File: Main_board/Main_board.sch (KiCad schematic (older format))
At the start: 29 parts, among them U1 ATmega328-AU, U2 74LVC2G08, U3 74LVC2G08, Y1 20Mhz

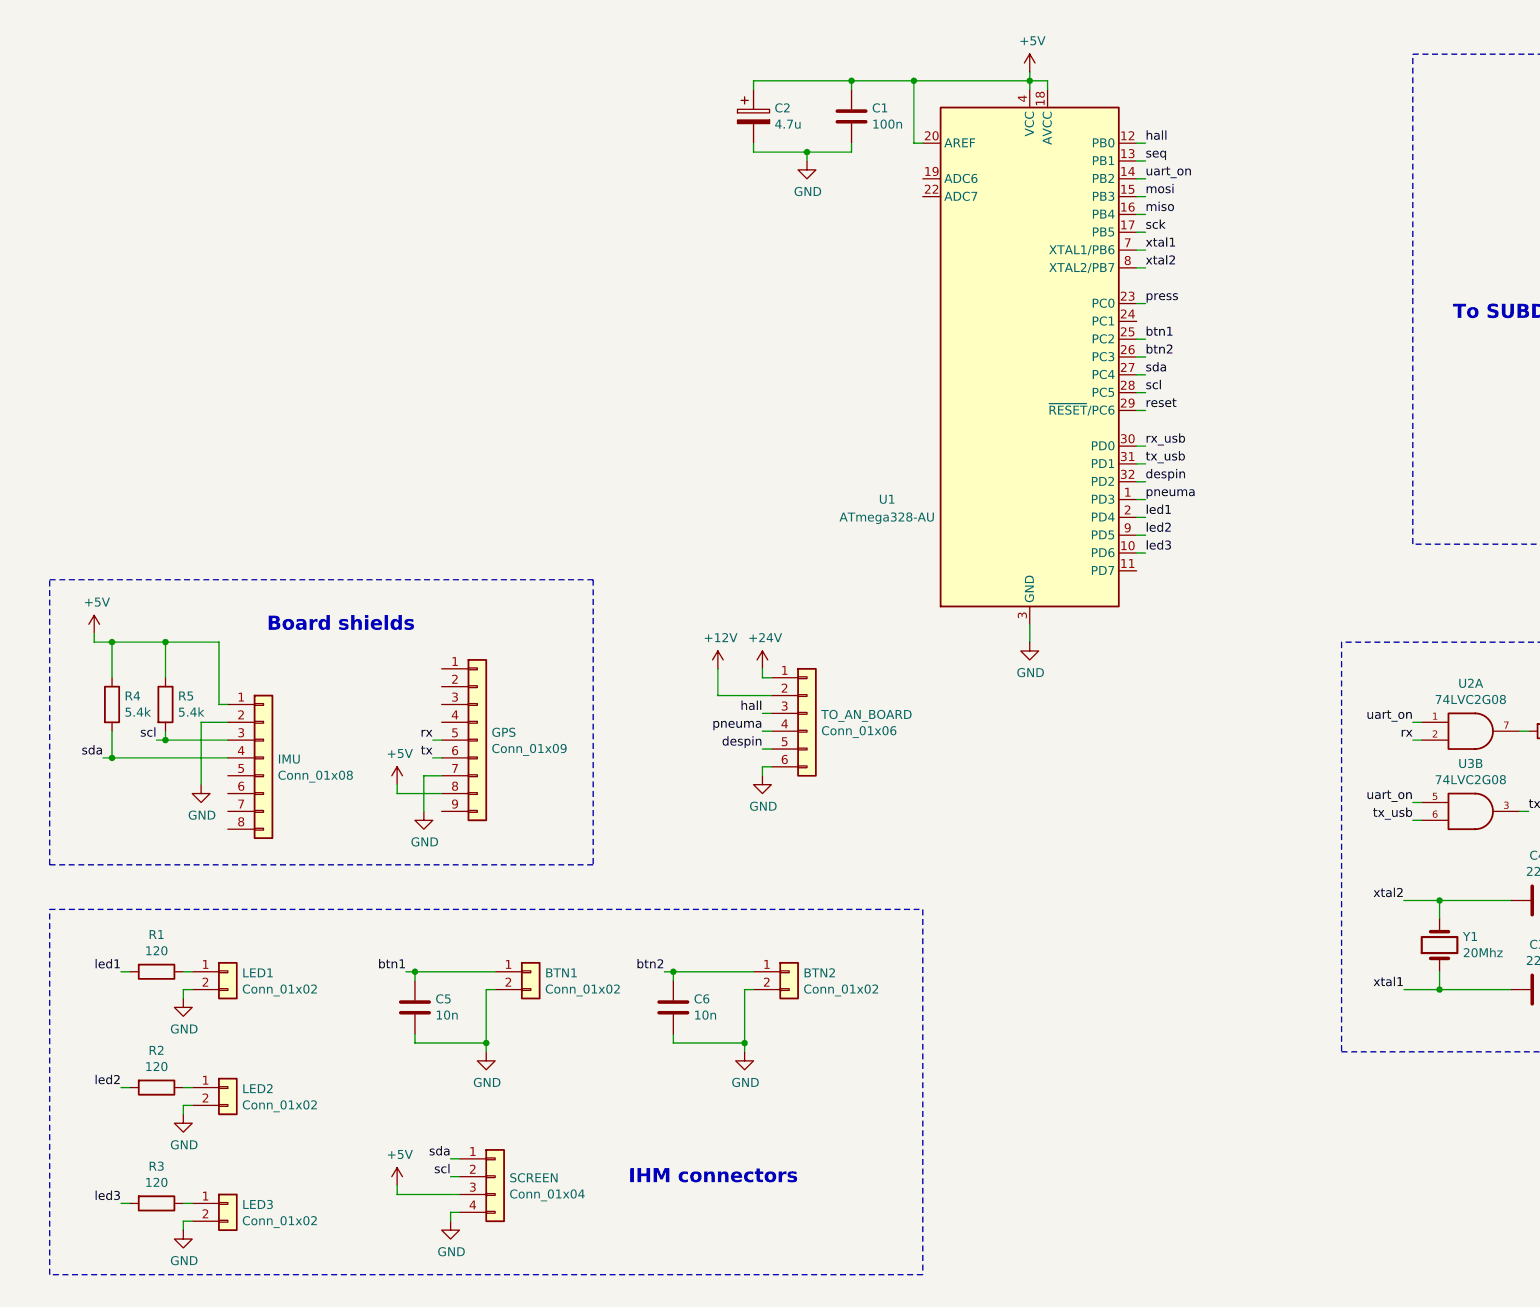
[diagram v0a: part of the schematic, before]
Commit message: ENH: Added VCO, voltage translator and flash chip libs and associated circuits
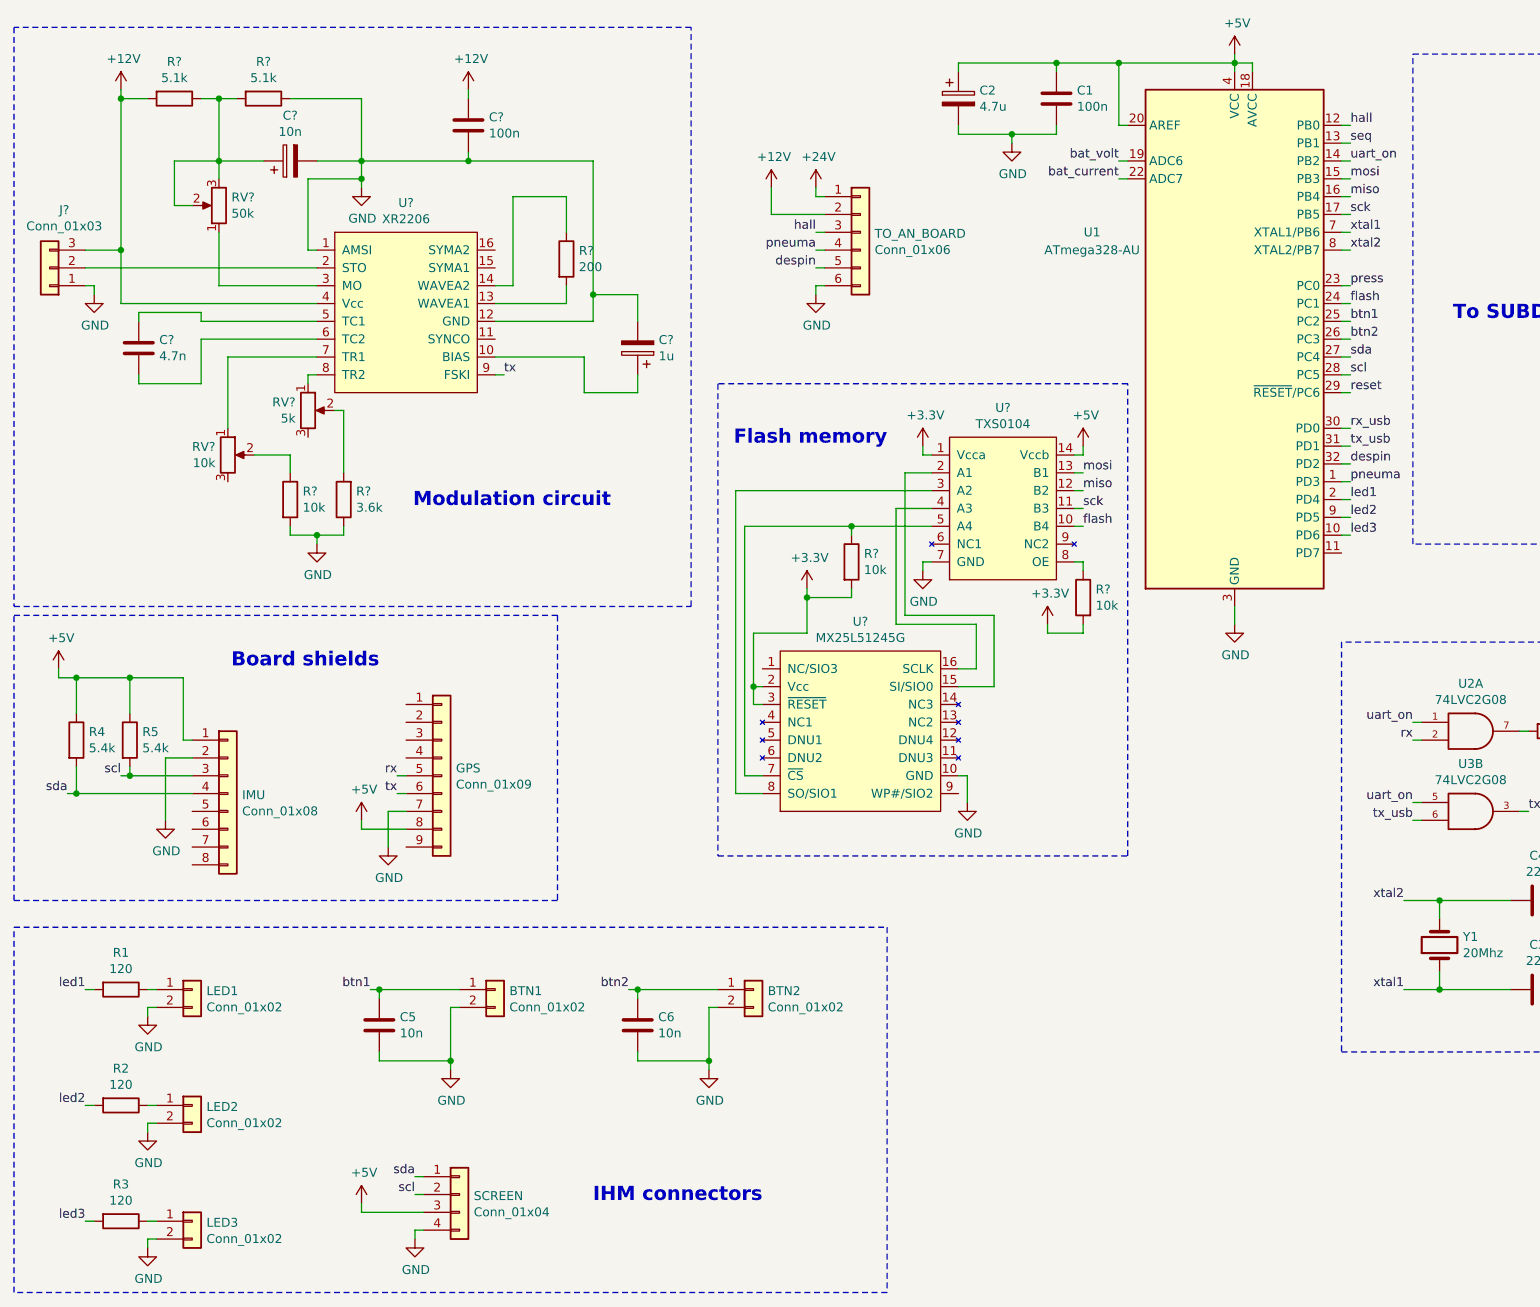
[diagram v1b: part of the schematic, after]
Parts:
- added C?: 4.7n, symbol Device:C
- added C?: 100n, symbol Device:C
- added C?: 1u, symbol Device:CP
- added C?: 10n, symbol Device:CP
- added J?: Conn_01x03, symbol Connector_Generic:Conn_01x03
- added R? (x2): 5.1k, symbol Device:R
- added R? (x3): 10k, symbol Device:R
- added R?: 3.6k, symbol Device:R
- added R?: 200, symbol Device:R
- added RV?: 5k, symbol Device:R_POT
- added RV?: 10k, symbol Device:R_POT
- added RV?: 50k, symbol Device:R_POT
- added U?: XR2206, Package_DIP:DIP-16_W7.62mm, symbol XR2206:XR2206
- added U?: TXS0104, Package_SO:SOIC-14_3.9x8.7mm_P1.27mm, symbol TXS0104:TXS0104
- added U?: MX25L51245G, Package_SO:SOIC-16W_7.5x10.3mm_P1.27mm, symbol MX25L51245G:MX25L51245G
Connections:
- net +12V: now also C?.1, J?.3 (Pin_3), R?.2, U?.4 (Vcc)
- net +5V: now also U?.14 (Vccb)
- net GND: now also C?.2, C?.2, C?.2, J?.1 (Pin_1), R?.1, R?.1, R?.2, U?.1 (AMSI), U?.10 (GND), U?.12 (GND), U?.7 (GND)
- net bat_current: now also U1.22 (ADC7)
- net bat_volt: now also U1.19 (ADC6)
- net miso: now also U?.12 (B2)
- net mosi: now also U?.13 (B1)
- net sck: now also U?.11 (B3)
- net tx: now also U?.9 (FSKI)
- net flash: now reaches U1.24 (PC1)
- net flash: now also U?.10 (B4)
- new net: C?.1, U?.10 (BIAS)
- new net: R?.2, U?.13 (WAVEA1)
- new net: R?.1, U?.14 (WAVEA2)
- new net: J?.2 (Pin_2), U?.2 (STO)
- new net: RV?.1, U?.3 (MO)
- new net: C?.1, U?.5 (TC1)
- new net: C?.2, U?.6 (TC2)
- new net: RV?.1, U?.7 (TR1)
- new net: RV?.1, U?.8 (TR2)
- new net: C?.1, R?.1, R?.2, RV?.2, RV?.3
- new net: R?.1, RV?.2
- new net: R?.2, RV?.2
- new net: U?.15 (SI/SIO0), U?.2 (A1)
- new net: U?.3 (A2), U?.8 (SO/SIO1)
- new net: U?.16 (SCLK), U?.4 (A3)
- new net: R?.1, U?.5 (A4), U?.7 (~CS)
- new net: R?.1, U?.8 (OE)
- new net +3V3: R?.2, R?.2, U?.1 (Vcca), U?.2 (Vcc), U?.3 (~RESET)
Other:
- note added: "Flash memory"
- note added: "Modulation circuit"
- moved on the sheet: BTN1, BTN2, C1, C2, C5, C6, GPS, IMU, LED1, LED2, LED3, R1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

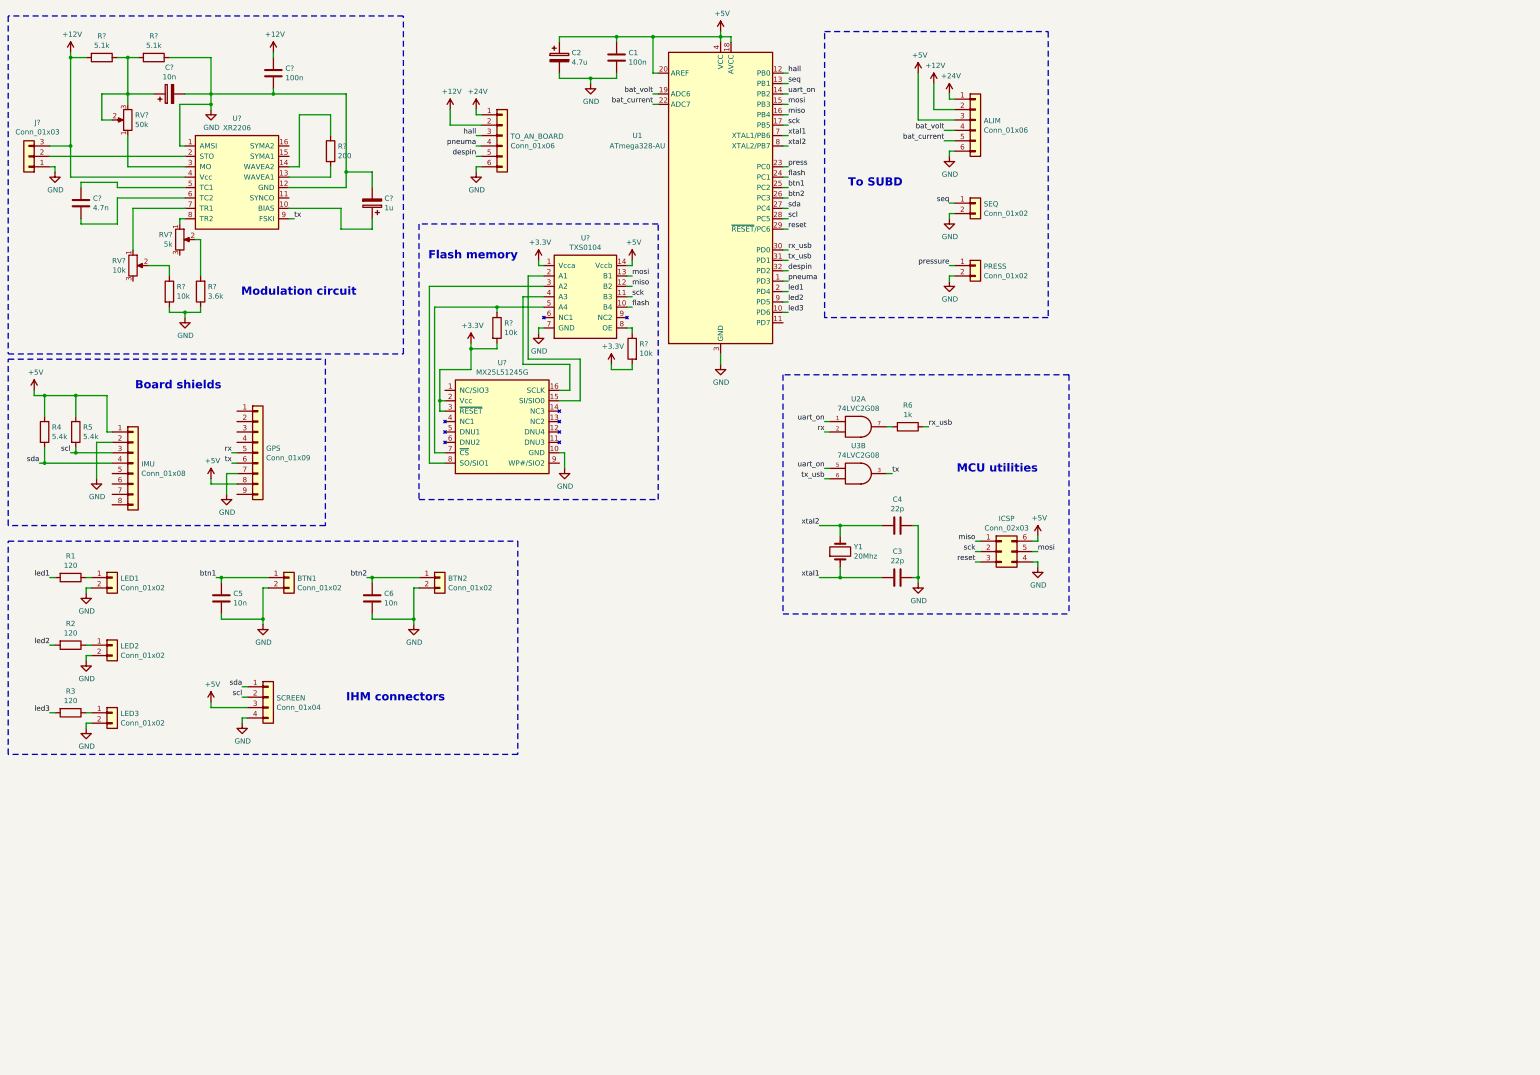
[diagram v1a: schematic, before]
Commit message: ENH: Added 12v_on + usb to ttl circuit
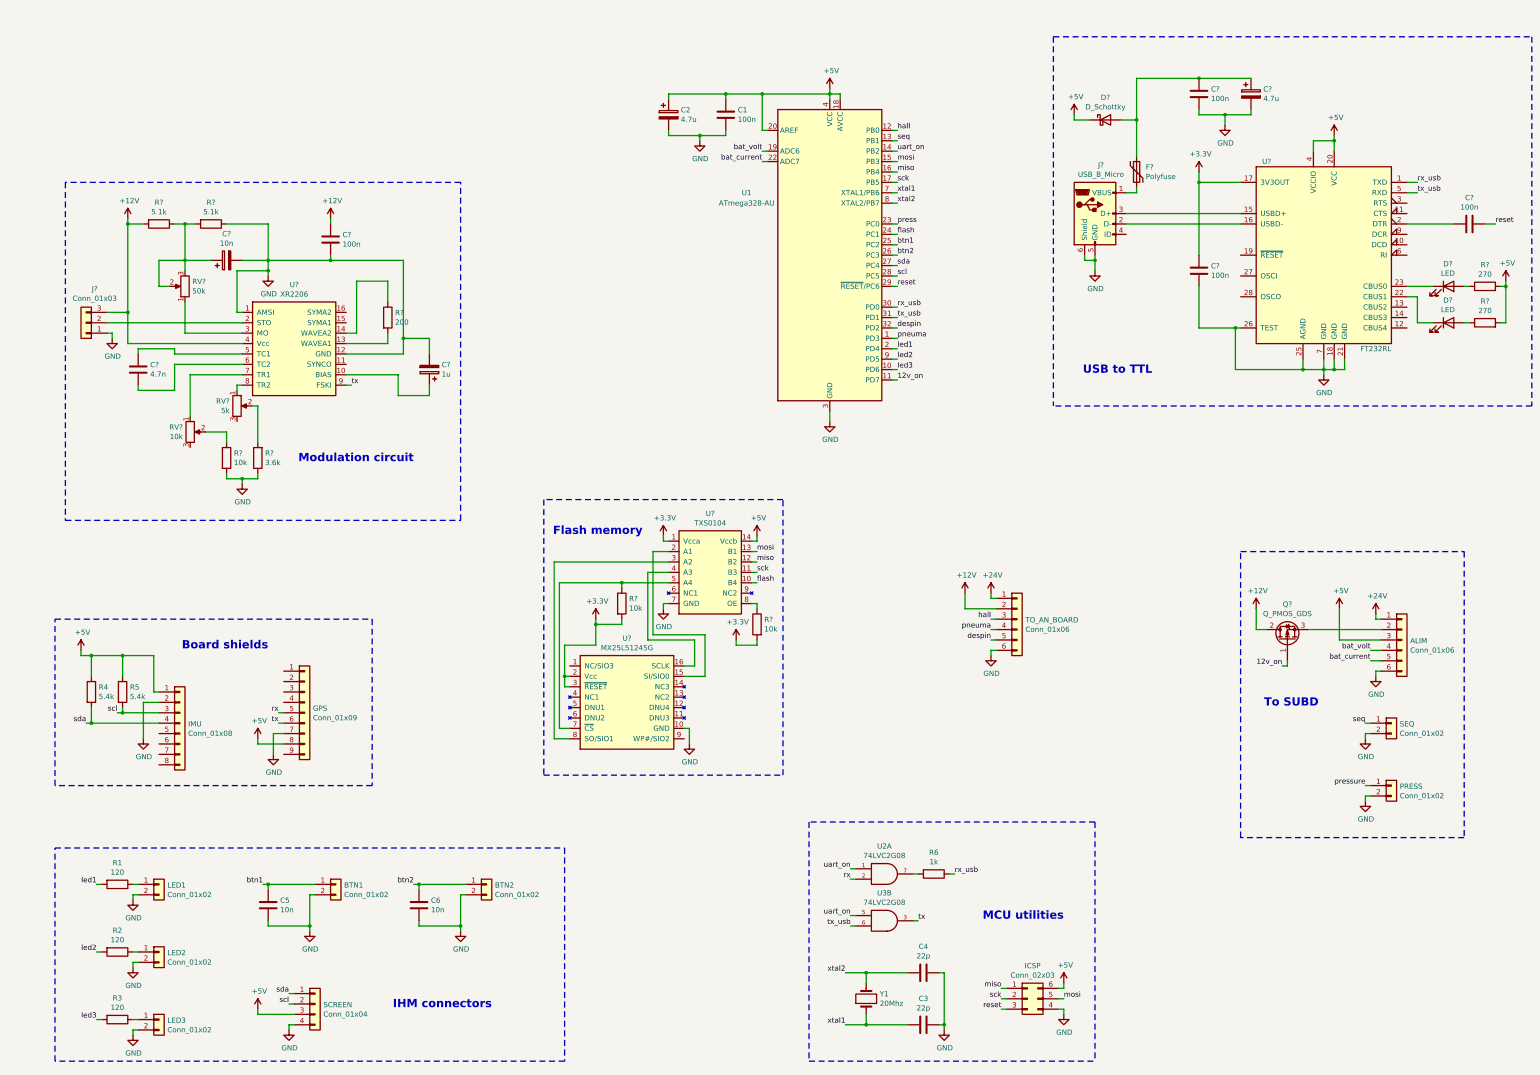
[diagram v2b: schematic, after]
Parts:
- added C? (x3): 100n, symbol Device:C
- added C?: 4.7u, symbol Device:CP
- added D? (x2): LED, symbol Device:LED
- added D?: D_Schottky, symbol Device:D_Schottky
- added F?: Polyfuse, symbol Device:Polyfuse
- added J?: USB_B_Micro, Connector_USB:USB_Micro-B_Molex-105017-0001, symbol Connector:USB_B_Micro
- added Q?: Q_PMOS_GDS, symbol Device:Q_PMOS_GDS
- added R? (x2): 270, symbol Device:R
- added U?: FT232RL, Package_SO:SSOP-28_5.3x10.2mm_P0.65mm, symbol Interface_USB:FT232RL
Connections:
- net +12V: now also Q?.2 (D); no longer ALIM.2 (Pin_2)
- net +3V3: now also C?.1, U?.17 (3V3OUT)
- net +5V: now also D?.1 (K), R?.2, R?.2, U?.20 (VCC), U?.4 (VCCIO)
- net GND: now also C?.2, C?.2, C?.2, J?.5 (GND), J?.6 (Shield), U?.18 (GND), U?.21 (GND), U?.25 (AGND), U?.26 (TEST), U?.7 (GND)
- net reset: now also C?.2
- net rx_usb: now also U?.1 (TXD)
- net tx_usb: now also U?.5 (RXD)
- net 12v_on: now reaches U1.11 (PD7)
- net 12v_on: now also Q?.1 (G)
- new net: ALIM.2 (Pin_2), Q?.3 (S)
- new net: J?.3 (D+), U?.15 (USBD+)
- new net: J?.2 (D-), U?.16 (USBD-)
- new net: C?.1, U?.2 (DTR)
- new net: D?.1 (K), U?.22 (CBUS1)
- new net: D?.1 (K), U?.23 (CBUS0)
- new net: D?.2 (A), R?.1 (x2)
- new net: C?.1, C?.1, D?.2 (A), F?.1
- new net: F?.2, J?.1 (VBUS)
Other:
- note added: "USB to TTL"
- moved on the sheet: ALIM, BTN1, BTN2, C1, C2, C3, C4, C5, C6, C?, GPS, ICSP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
